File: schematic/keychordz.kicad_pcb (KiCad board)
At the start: 2 copper layers, 100 x 100 mm, 54 parts, among them IC1 MCP73833-BZI_UN, J1 USB_C_Receptacle_USB2.0, J2 Conn_01x04_Male, SW1 SW_Push, SW2 SW_Push, SW3 SW_Push, SW4 SW_Push, SW5 SW_Push, SW6 SW_Push, SW7 SW_Push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

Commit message: add Breakout
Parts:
- added C25: LED, Capacitor_SMD:C_0603_1608Metric_Pad1.08x0.95mm_HandSolder, F.Cu at (42.5, 92.5)
- added C26: LED, Capacitor_SMD:C_0603_1608Metric_Pad1.08x0.95mm_HandSolder, F.Cu at (24.5, 78.3)
- added C27: LED, Capacitor_SMD:C_0603_1608Metric_Pad1.08x0.95mm_HandSolder, F.Cu at (55.2, 51.3)
- added C28: LED, Capacitor_SMD:C_0603_1608Metric_Pad1.08x0.95mm_HandSolder, F.Cu at (79.7, 42.4)
- added C29: LED, Capacitor_SMD:C_0603_1608Metric_Pad1.08x0.95mm_HandSolder, F.Cu at (102.4, 50.2)
- added C30: LED, Capacitor_SMD:C_0603_1608Metric_Pad1.08x0.95mm_HandSolder, F.Cu at (124.3, 60.1)
- added C4: LED, Capacitor_SMD:C_0603_1608Metric_Pad1.08x0.95mm_HandSolder, F.Cu at (16.9, 91.7)
- added D10: WS2812B, LED_SMD:LED_WS2812B_PLCC4_2.2x2.2mm, F.Cu at (128.2, 64.9)
- added D4: WS2812B, LED_SMD:LED_WS2812B_PLCC4_2.2x2.2mm, F.Cu at (25.3, 97.3)
- added D5: WS2812B, LED_SMD:LED_WS2812B_PLCC4_2.2x2.2mm, F.Cu at (42.8, 98.6)
- added D6: WS2812B, LED_SMD:LED_WS2812B_PLCC4_2.2x2.2mm, F.Cu at (33.1, 83.1)
- added D7: WS2812B, LED_SMD:LED_WS2812B_PLCC4_2.2x2.2mm, F.Cu at (59.1, 55.9)
- added D8: WS2812B, LED_SMD:LED_WS2812B_PLCC4_2.2x2.2mm, F.Cu at (84.1, 47.0)
- added D9: WS2812B, LED_SMD:LED_WS2812B_PLCC4_2.2x2.2mm, F.Cu at (106.3, 54.9)
- added SW9: SW_SPST, Button_Switch_THT:SW_DIP_SPSTx02_Slide_6.7x6.64mm_W7.62mm_P2.54mm_LowProfile, F.Cu at (57.7, 37.1)
- AE1: footprint RF_Antenna:Texas_SWRA117D_2.4GHz_Left -> RF_Antenna:Texas_SWRA117D_2.4GHz_Right
- moved C6 134.4 mm to (31.8, 55.8), turned to 0 degrees
- moved C19 131.6 mm to (31.8, 53.2), turned to 180 degrees
- moved L4 129.0 mm to (32.8, 50.0), turned to 180 degrees
- moved C20 125.7 mm to (32.8, 46.9), turned to 180 degrees
- moved C17 125.1 mm to (22.6, 54.2), turned to 0 degrees
- moved C21 122.8 mm to (32.4, 44.4), turned to 180 degrees
- moved C18 122.0 mm to (24.6, 50.2), turned to 90 degrees
- moved X2 120.4 mm to (22.6, 50.3), turned to -90 degrees
- moved C7 119.1 mm to (32.3, 41.0), turned to 0 degrees
- moved C8 116.6 mm to (32.3, 38.5), turned to 0 degrees
- moved C5 115.9 mm to (20.1, 48.1), turned to -90 degrees
- moved C14 114.1 mm to (18.5, 47.6), turned to -90 degrees
- moved U1 112.4 mm to (24.6, 41.5), turned to 90 degrees
- moved L2 108.7 mm to (17.0, 44.1), turned to 180 degrees
- moved C16 106.1 mm to (18.0, 41.0), turned to 90 degrees
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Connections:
- BT1 pad 1: V_BAT -> V_BAT_SW
- C23 pad 1: V_BAT -> V_BAT_SW
- IC1 pad 10: V_BAT -> V_BAT_SW
- IC1 pad 9: V_BAT -> V_BAT_SW
- SW1 pad 1: GND -> Net-(SW1-Pad1)
- SW1 pad 2: Net-(SW1-Pad2) -> GND
- SW2 pad 1: GND -> Net-(SW2-Pad1)
- SW2 pad 2: Net-(SW2-Pad2) -> GND
- SW3 pad 1: GND -> Net-(SW3-Pad1)
- SW3 pad 2: Net-(SW3-Pad2) -> GND
- SW4 pad 1: GND -> Net-(SW4-Pad1)
- SW4 pad 2: Net-(SW4-Pad2) -> GND
- SW5 pad 1: GND -> Net-(SW5-Pad1)
- SW5 pad 2: Net-(SW5-Pad2) -> GND
- SW6 pad 1: GND -> Net-(SW6-Pad1)
- SW6 pad 2: Net-(SW6-Pad2) -> GND
- SW7 pad 1: GND -> Net-(SW7-Pad1)
- SW7 pad 2: Net-(SW7-Pad2) -> GND
- U1 pad AC11: Net-(SW4-Pad2) -> Net-(SW4-Pad1)
- U1 pad AC15: Net-(SW6-Pad2) -> Net-(SW2-Pad1)
- U1 pad AC17: unconnected-(U1-PadAC17) -> Net-(D10-Pad4)
- U1 pad AC9: Net-(SW2-Pad2) -> Net-(SW6-Pad1)
- U1 pad AD10: Net-(SW3-Pad2) -> Net-(SW5-Pad1)
- U1 pad AD12: Net-(SW5-Pad2) -> Net-(SW3-Pad1)
- U1 pad AD16: Net-(SW7-Pad2) -> Net-(SW1-Pad1)
- U1 pad AD8: Net-(SW1-Pad2) -> Net-(SW7-Pad1)
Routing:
- net RST: track 0.00 -> 4.06 mm, vias 0 -> 2
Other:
- board size 100 x 100 mm -> 126.7 x 100 mm
- copper layers 2 -> 4

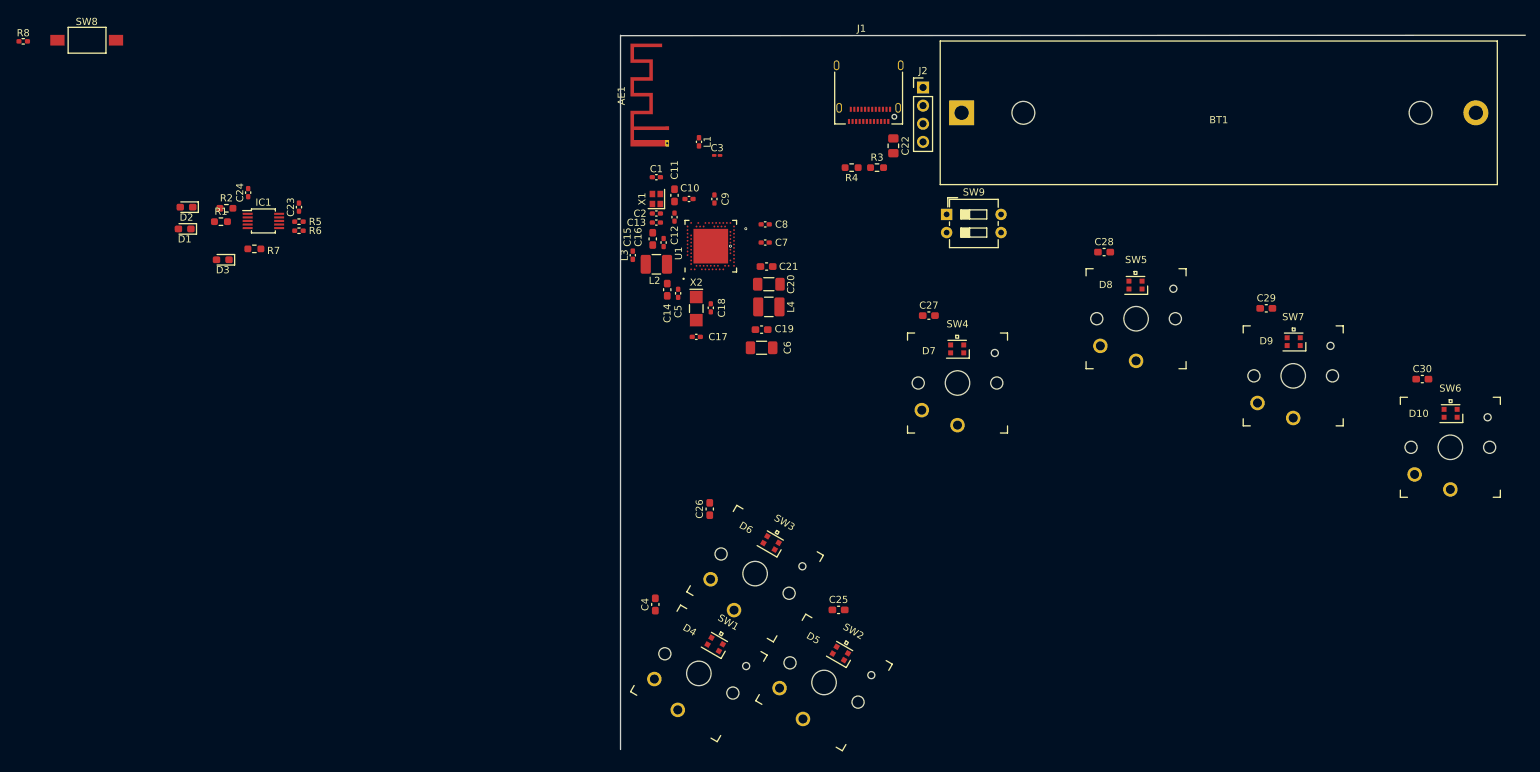
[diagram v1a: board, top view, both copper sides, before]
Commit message: keyboard schematic with breakout
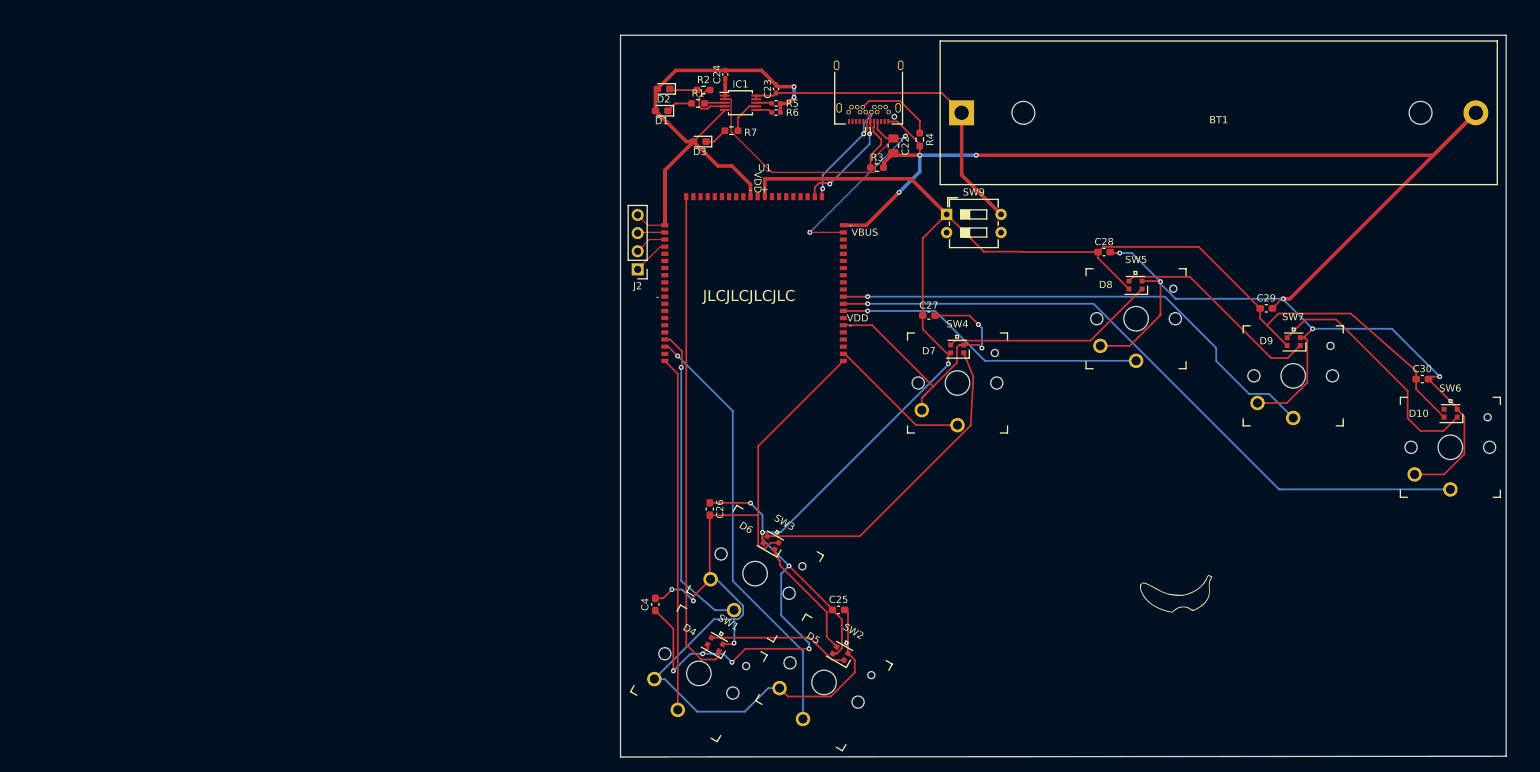
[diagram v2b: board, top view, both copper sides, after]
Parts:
- removed AE1: PCB, RF_Antenna:Texas_SWRA117D_2.4GHz_Right
- removed C1, C17, C18, C2: 12pF, Capacitor_SMD:C_0402_1005Metric_Pad0.74x0.62mm_HandSolder
- removed C10, C13: nc, Capacitor_SMD:C_0402_1005Metric_Pad0.74x0.62mm_HandSolder
- removed C11: 100pF, Capacitor_SMD:C_0603_1608Metric_Pad1.08x0.95mm_HandSolder
- removed C12, C5, C7, C8: 100nF, Capacitor_SMD:C_0402_1005Metric_Pad0.74x0.62mm_HandSolder
- removed C14, C15: 1µF, Capacitor_SMD:C_0603_1608Metric_Pad1.08x0.95mm_HandSolder
- removed C16: 47nF, Capacitor_SMD:C_0402_1005Metric_Pad0.74x0.62mm_HandSolder
- removed C19, C21: 4.7µF, Capacitor_SMD:C_0603_1608Metric_Pad1.08x0.95mm_HandSolder
- removed C20, C6: 4.7µF, Capacitor_SMD:C_1206_3216Metric_Pad1.33x1.80mm_HandSolder
- removed C3: 0.8pF, Capacitor_SMD:C_0201_0603Metric_Pad0.64x0.40mm_HandSolder
- removed C9: 820pF, Capacitor_SMD:C_0402_1005Metric_Pad0.74x0.62mm_HandSolder
- removed L1: 3.9nH, Inductor_SMD:L_0402_1005Metric_Pad0.77x0.64mm_HandSolder
- removed L2, L4: 10µH, Inductor_SMD:L_1210_3225Metric_Pad1.42x2.65mm_HandSolder
- removed L3: 15nH, Inductor_SMD:L_0402_1005Metric_Pad0.77x0.64mm_HandSolder
- removed R8: 10k, Resistor_SMD:R_0402_1005Metric_Pad0.72x0.64mm_HandSolder
- removed SW8: SW_Push, Button_Switch_SMD:SW_SPST_PTS636
- removed X1: 32MHz, Crystal:Crystal_SMD_2016-4Pin_2.0x1.6mm
- removed X2: 32.768kHz, Crystal:Crystal_SMD_MicroCrystal_CC7V-T1A-2Pin_3.2x1.5mm_HandSoldering
- added G***: LOGO, LOGO, F.Cu at (89.7, 90.0)
- J1: footprint Connector_USB:USB_C_Receptacle_Amphenol_12401610E4-2A -> Connector_USB:USB_C_Receptacle_Amphenol_12401548E4-2A
- U1: value nRF52840 -> nRF52840_Breakout; footprint Package_DFN_QFN:Nordic_AQFN-73-1EP_7x7mm_P0.5mm -> schematic:nRF52840_Breakout
- moved C23 68.8 mm to (33.8, 19.5)
- moved D3 68.8 mm to (23.1, 26.9)
- moved R5 68.8 mm to (33.8, 21.6)
- moved R6 68.8 mm to (33.8, 22.8)
- moved C24 68.8 mm to (26.7, 17.5)
- moved D1 68.8 mm to (17.8, 22.6)
- moved D2 68.8 mm to (18.0, 19.5)
- moved IC1 68.8 mm to (28.8, 21.4)
- moved R1 68.8 mm to (22.9, 21.6)
- moved R2 68.8 mm to (23.6, 19.7)
- moved R7 68.8 mm to (27.5, 25.4)
- moved J2 47.4 mm to (14.4, 44.8), turned to 180 degrees
- moved R4 10.3 mm to (53.9, 26.6), turned to -90 degrees
- moved U1 9.54 mm to (31.2, 34.6), turned to 0 degrees
- turned C26 to -90 degrees
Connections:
- D10 pad 4: Net-(D10-Pad4) -> unconnected-(D10-Pad4)
- D4 pad 2: unconnected-(D4-Pad2) -> Net-(U1-PadAD22)
- J2 pad 1: SWDIO -> SWDCLK
- J2 pad 2: SWDCLK -> SWDIO
- SW1 pad 1: Net-(SW1-Pad1) -> Net-(U1-PadB11)
- SW2 pad 1: Net-(SW2-Pad1) -> Net-(U1-PadA14)
- SW3 pad 1: Net-(SW3-Pad1) -> Net-(U1-PadB15)
- SW4 pad 1: Net-(SW4-Pad1) -> Net-(U1-PadA8)
- SW5 pad 1: Net-(SW5-Pad1) -> Net-(U1-PadG1)
- SW6 pad 1: Net-(SW6-Pad1) -> Net-(U1-PadH2)
- SW7 pad 1: Net-(SW7-Pad1) -> Net-(U1-PadJ1)
- U1 pad A14: unconnected-(U1-PadA14) -> Net-(U1-PadA14)
- U1 pad A8: unconnected-(U1-PadA8) -> Net-(U1-PadA8)
- U1 pad AC11: Net-(SW4-Pad1) -> unconnected-(U1-PadAC11)
- U1 pad AC15: Net-(SW2-Pad1) -> unconnected-(U1-PadAC15)
- U1 pad AC17: Net-(D10-Pad4) -> unconnected-(U1-PadAC17)
- U1 pad AC9: Net-(SW6-Pad1) -> unconnected-(U1-PadAC9)
- U1 pad AD10: Net-(SW5-Pad1) -> unconnected-(U1-PadAD10)
- U1 pad AD12: Net-(SW3-Pad1) -> unconnected-(U1-PadAD12)
- U1 pad AD16: Net-(SW1-Pad1) -> unconnected-(U1-PadAD16)
- U1 pad AD22: unconnected-(U1-PadAD22) -> Net-(U1-PadAD22)
- U1 pad AD8: Net-(SW7-Pad1) -> unconnected-(U1-PadAD8)
- U1 pad B1: VDD -> unconnected-(U1-PadB1)
- U1 pad B11: unconnected-(U1-PadB11) -> Net-(U1-PadB11)
- U1 pad B15: unconnected-(U1-PadB15) -> Net-(U1-PadB15)
- U1 pad G1: unconnected-(U1-PadG1) -> Net-(U1-PadG1)
- U1 pad H2: unconnected-(U1-PadH2) -> Net-(U1-PadH2)
- U1 pad J1: unconnected-(U1-PadJ1) -> Net-(U1-PadJ1)
- U1 pad W1: VDD -> unconnected-(U1-PadW1)
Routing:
- net GND: track 0.00 -> 514.6 mm, vias 0 -> 15
- net V_BAT: track 0.00 -> 267.5 mm, vias 0 -> 8
- net Net-(U1-PadH2): track 0.00 -> 95.7 mm, vias 0 -> 1
- net Net-(U1-PadJ1): track 0.00 -> 71.1 mm, vias 0 -> 1
- net Net-(U1-PadAD22): track 0.00 -> 69.0 mm
- net +5V: track 0.00 -> 66.0 mm, vias 0 -> 2
- net Net-(U1-PadA14): track 0.00 -> 60.4 mm, vias 0 -> 1
- net Net-(U1-PadB11): track 0.00 -> 49.6 mm
- net V_BAT_SW: track 0.00 -> 47.1 mm
- net Net-(D6-Pad4): track 0.00 -> 45.3 mm
- net Net-(U1-PadB15): track 0.00 -> 44.2 mm, vias 0 -> 1
- net Net-(U1-PadG1): track 0.00 -> 43.9 mm, vias 0 -> 1
- net Net-(D10-Pad2): track 0.00 -> 34.3 mm
- net Net-(D7-Pad4): track 0.00 -> 30.0 mm
- net Net-(D8-Pad4): track 0.00 -> 29.7 mm
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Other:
- board size 126.7 x 100 mm -> 124 x 101 mm
- copper layers 4 -> 2
- board text added: "JLCJLCJLCJLC"

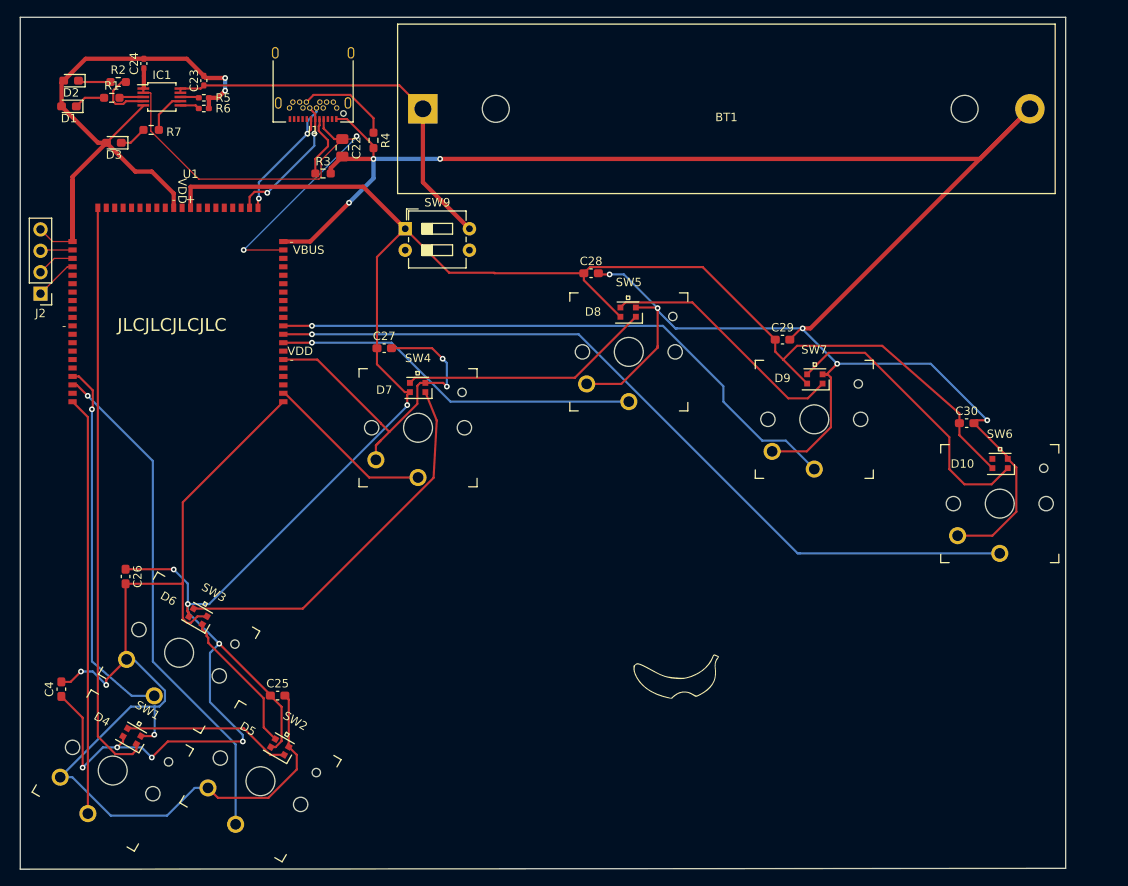
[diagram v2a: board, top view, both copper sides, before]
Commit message: update breakout without castellations
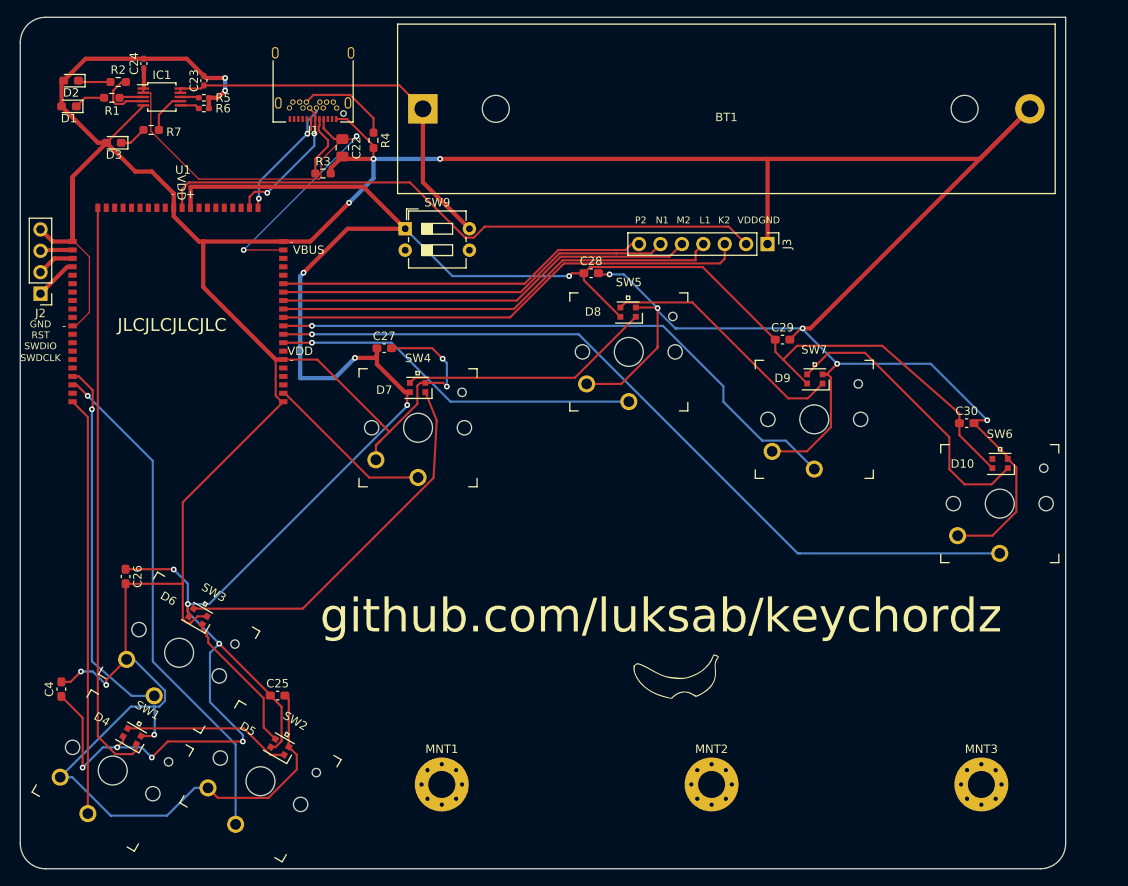
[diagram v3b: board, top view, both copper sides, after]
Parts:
- added J3: Conn_01x04_Male, Connector_PinHeader_2.54mm:PinHeader_1x07_P2.54mm_Vertical, F.Cu at (100.6, 38.9)
- added MNT1: MountingHole_3.2mm_M3_Pad_Via, MountingHole:MountingHole_3.2mm_M3_Pad_Via, F.Cu at (62.0, 103.0)
- added MNT2: MountingHole_3.2mm_M3_Pad_Via, MountingHole:MountingHole_3.2mm_M3_Pad_Via, F.Cu at (94.0, 103.0)
- added MNT3: MountingHole_3.2mm_M3_Pad_Via, MountingHole:MountingHole_3.2mm_M3_Pad_Via, F.Cu at (126.0, 103.0)
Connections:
- U1 pad B1: unconnected-(U1-PadB1) -> Net-(J3-Pad2)
- U1 pad K2: unconnected-(U1-PadK2) -> Net-(U1-PadK2)
- U1 pad L1: unconnected-(U1-PadL1) -> Net-(J3-Pad4)
- U1 pad M2: unconnected-(U1-PadM2) -> Net-(U1-PadM2)
- U1 pad N1: unconnected-(U1-PadN1) -> Net-(U1-PadN1)
- U1 pad P2: unconnected-(U1-PadP2) -> Net-(U1-PadP2)
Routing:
- net Net-(J3-Pad2): track 0.00 -> 73.6 mm
- net GND: track 514.6 -> 575.9 mm
- net Net-(U1-PadK2): track 0.00 -> 57.0 mm
- net Net-(J3-Pad4): track 0.00 -> 53.6 mm
- net Net-(U1-PadM2): track 0.00 -> 50.1 mm
- net Net-(U1-PadN1): track 0.00 -> 47.1 mm
- net Net-(U1-PadP2): track 0.00 -> 44.1 mm
- net V_BAT: track 267.5 -> 290.3 mm, vias 8 -> 11
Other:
- outline, holes or cut-outs redrawn
- board text added: "GND"
- board text added: "K2"
- board text added: "L1"
- board text added: "M2"
- board text added: "N1"
- board text added: "P2"
- board text added: "RST"
- board text added: "SWDCLK"
- board text added: "SWDIO"
- board text added: "VDD"
- board text added: "github.com/luksab/keychordz"
